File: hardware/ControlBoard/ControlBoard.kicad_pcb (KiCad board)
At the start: 4 copper layers, 95 x 95 mm, 172 parts, among them J1 Lamp 1 Out, J10 CAN, J11 USB_B_Micro, J12 Conn_01x02, J13 Available GPIO, J14 MOTOR_CTRL1, J15 MOTOR_CTRL2, J2 ESTOP1, J3 ESTOP2, J4 Lamp 3 Out, J5 Lamp 2 Out, J6 Lamp 4 Out, J7 PWR_IN, J8 USB_B_Micro, J9 UART BACKUP, Q1 DMN62D0U-13, Q2 DMN62D0U-13, Q3 DMN62D0U-13, Q4 DMN62D0U-13, Q5 SS8050-G, Q6 SS8050-G, SW1 SW_Push, SW2 SW_Push, U1 CP2102N-A02-GQFN28, U10 74LVC1G17W5-7, U11 74LVC1G17W5-7, U12 TXU0104QPWRQ1, U2 Lora_Module, U3 L4941BV, U4 LD1086V33-DG, U5 ESP32-S3-WROOM-1U-N16, U6 74LVC1G97W6-7, U7 SN65HVD232, U8 SN74LVC1GU04DBVR, U9 TXU0104QPWRQ1

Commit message: Power Board Changes
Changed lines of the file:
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@@
     (property "Sheetname" "")
     (attr smd)
-    (fp_text reference "SW1" (at -1.625 2.48 180) (layer "F.SilkS")
+    (fp_text reference "SW1" (at -0.675 3.355 180) (layer "F.SilkS")
       (effects (font (size 1 1) (thickness 0.15)))
     )

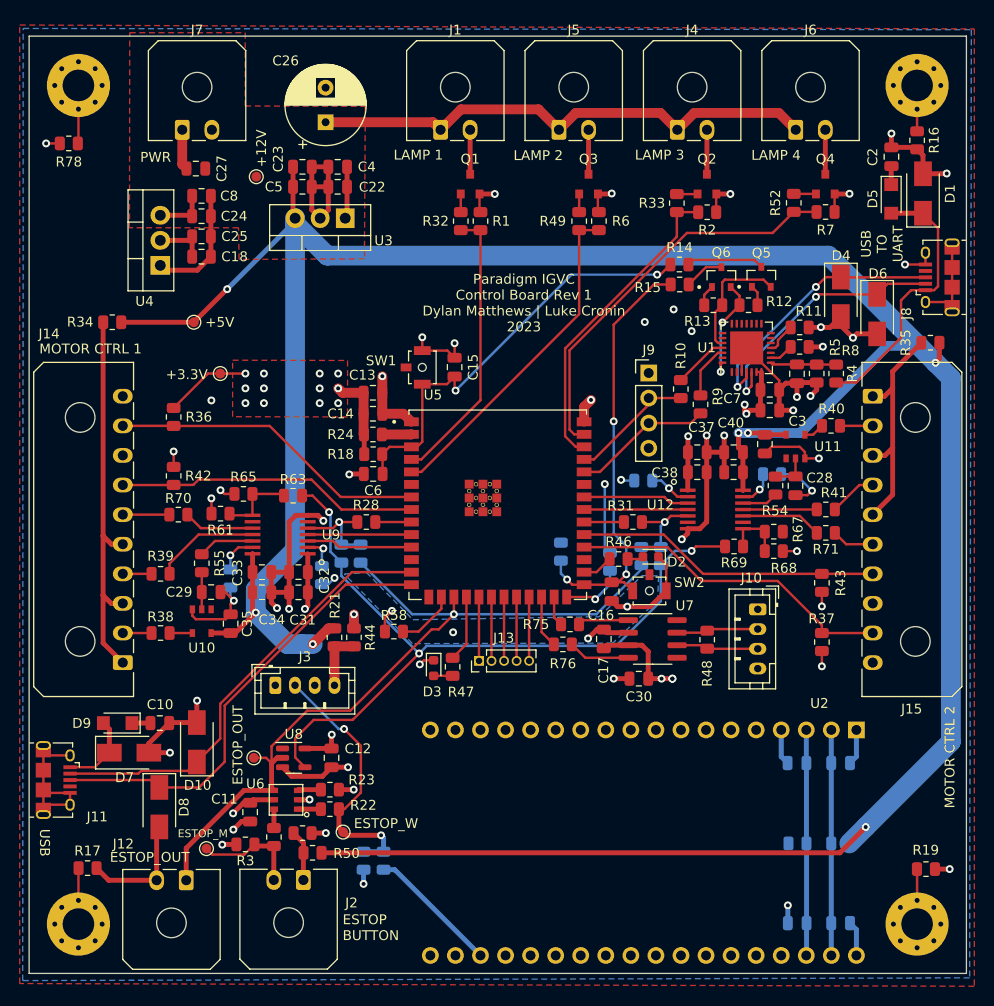
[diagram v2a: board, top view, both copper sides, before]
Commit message: Power Board Schematic Revision Done, Fix Lora Symbol and Update Control Board Routing
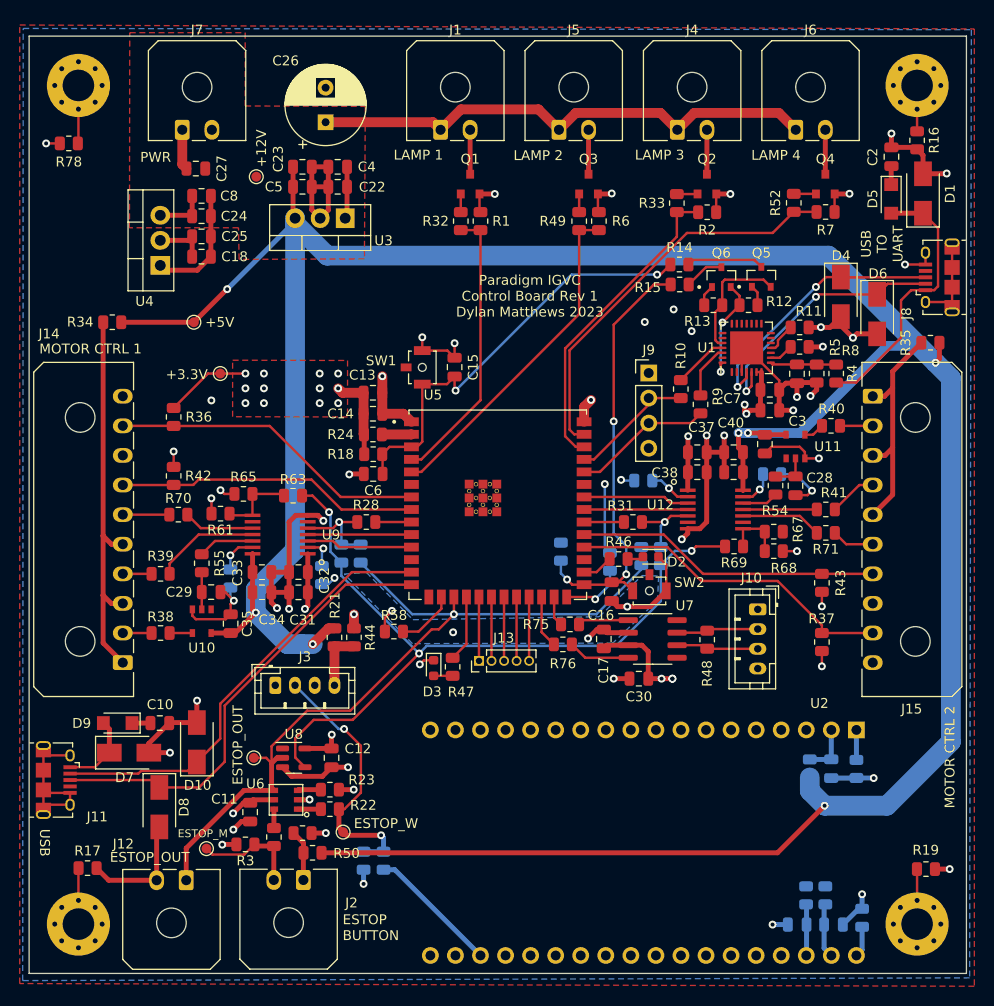
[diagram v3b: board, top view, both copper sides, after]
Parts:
- removed C20: 0.1u, Capacitor_SMD:C_0805_2012Metric
- removed G***: LOGO, controlLib:Paradigm_NameBelow_25.4mm
- removed REF** (x2): 577102B00000G_HEATSINK, controlLib:577102B00000G_HEATSINK
- added R72: 0, Resistor_SMD:R_0805_2012Metric, B.Cu at (133.8, 124.3)
- added R74: 0, Resistor_SMD:R_0805_2012Metric, B.Cu at (134.4, 139.4)
- added R77: 0, Resistor_SMD:R_0805_2012Metric, B.Cu at (130.7, 137.1)
- moved C19 16.8 mm to (131.5, 140.1), turned to 180 degrees
- moved R20 8.20 mm to (129.1, 124.2), turned to 90 degrees
- moved R45 5.33 mm to (128.8, 137.1), turned to -90 degrees
- moved C9 1.11 mm to (131.3, 124.2), turned to 90 degrees
- moved C21 0.15 mm to (127.8, 140.1)
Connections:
- C19 pad 2: /3V3_LORA -> /3V3_LORA_A
- C21 pad 2: /3V3_LORA -> /3V3_LORA_B
- R45 pad 2: /3V3_LORA -> /3V3_LORA_B
- U2 pad 1: GND -> Net-(U2-Pad1)
- U2 pad 19: GND -> Net-(U2-Pad19)
- U2 pad 20: /5V_LORA -> /3V3_LORA_A
- U2 pad 21: /3V3_LORA -> /3V3_LORA_B
- U2 pad 3: /3V3_LORA -> unconnected-(U2-Pad3)
- U2 pad 4: GND -> unconnected-(U2-Pad4)
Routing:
- net /3V3_LORA: track 22.9 -> 0.00 mm
- net /5V_LORA: track 22.9 -> 5.16 mm
- net /3V3_LORA_A: track 0.00 -> 5.54 mm
- net /3V3_LORA_B: track 0.00 -> 5.14 mm
- net Net-(U2-Pad19): track 0.00 -> 3.14 mm
- net Net-(U2-Pad1): track 0.00 -> 3.04 mm
- net GND: track 272.6 -> 269.9 mm, vias 50 -> 52
- net +5V: track 305.8 -> 306.9 mm
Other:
- board text added: "Paradigm IGVC Control Board Rev 1 Dylan Matthews 2023"
- board text removed: "Paradigm IGVC Control Board Rev 1 Dylan Matthews | Luke Cronin 2023"

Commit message: PDB routing V2 first pass
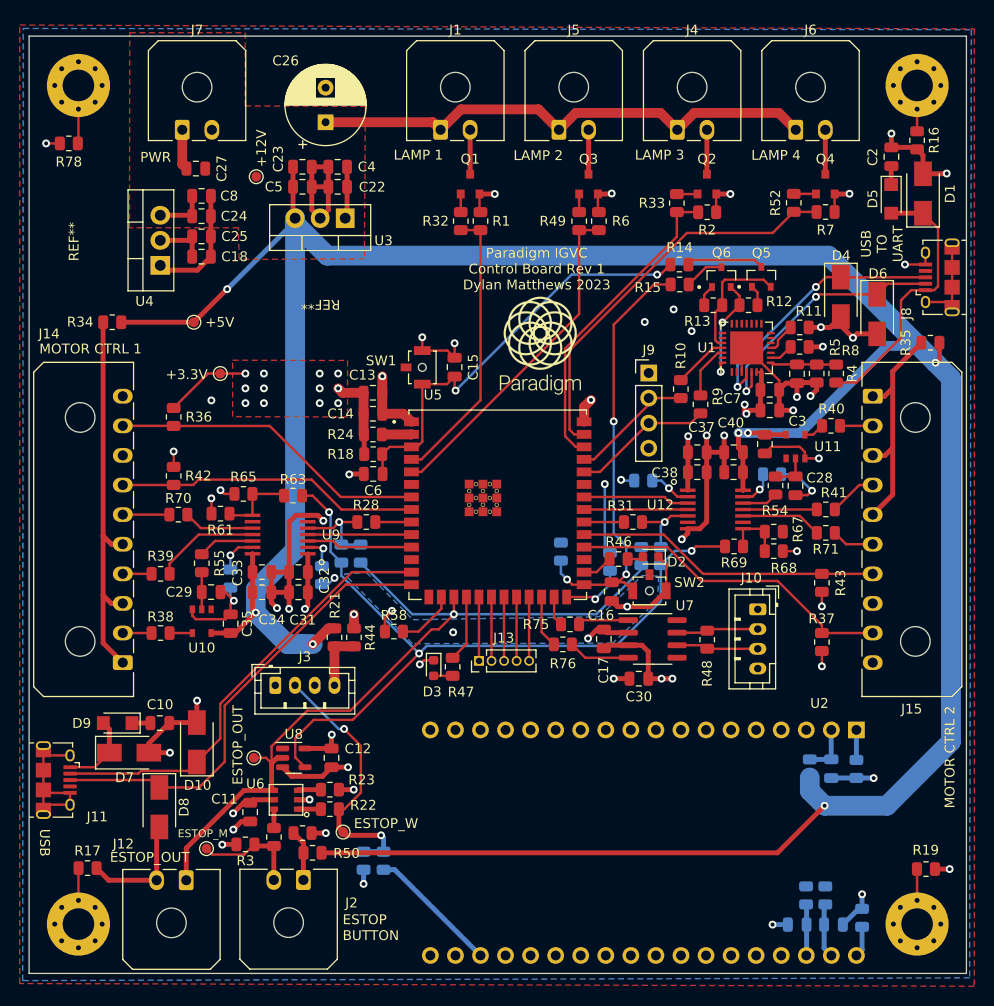
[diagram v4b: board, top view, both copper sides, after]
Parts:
- added G***: LOGO, controlLib:Paradigm_NameBelow_12.7mm, F.Cu at (101.8, 81.4)
- added REF**: 577102B00000G_HEATSINK, controlLib:577102B00000G_HEATSINK, F.Cu at (79.5, 76.7)
- added REF**: 577102B00000G_HEATSINK, controlLib:577102B00000G_HEATSINK, F.Cu at (55.0, 70.8)
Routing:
- net +3V3: vias 30 -> 29
